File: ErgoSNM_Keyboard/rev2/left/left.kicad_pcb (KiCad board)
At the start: 2 copper layers, 117.5 x 106.7 mm, 113 parts, among them J1 USB_C_Receptacle_USB2.0, J2 Conn_01x10, J3 Conn_01x08, J4 Conn_01x08, Q1 BSS138, SW1 BOOT, SW2 RESET, U1 SRV05-4, U2 RT9013-33GB, U3 RP2040, U4 W25Q128JVS, Y1 12MHz

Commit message: Update rev2
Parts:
- removed the C3 at (66.4, 39.4)
- removed the H4 at (138.4, 88.3)
- removed H7, H9: MountingHole, MountingHole:MountingHole_2.2mm_M2
- removed JP1: SolderJumper_3_Bridged12, Jumper:SolderJumper-3_P1.3mm_Bridged12_Pad1.0x1.5mm_NumberLabels
- removed LD1: SK6812MINI-E, ErgoSNM_Keyboard:SK6812MINI-E
- removed Q1: BSS138, Package_TO_SOT_SMD:SOT-23
- removed the R3 at (83.4, 40.3)
- removed the R4 at (78.1, 40.3)
- added TP4: TestPoint, TestPoint:TestPoint_Pad_D2.5mm, B.Cu at (64.6, 39.1)
- J2: footprint Connector_PinSocket_2.54mm:PinSocket_1x10_P2.54mm_Vertical -> Connector_PinSocket_2.54mm:PinSocket_1x08_P2.54mm_Vertical
- J3: footprint Connector_PinSocket_2.00mm:PinSocket_1x08_P2.00mm_Vertical -> Connector_PinSocket_2.00mm:PinSocket_2x04_P2.00mm_Vertical
- J4: footprint ErgoSNM_Keyboard:FPC_8P_0.5mm -> ErgoSNM_Keyboard:FPC_8P_1.0mm
- TP3: footprint TestPoint:TestPoint_Pad_D2.0mm -> TestPoint:TestPoint_Pad_D2.5mm
- moved R8 114.9 mm to (87.2, 34.2), turned to 0 degrees
- moved C7 113.5 mm to (87.2, 35.2), turned to 180 degrees
- moved C6 112.5 mm to (86.1, 37.2), turned to 0 degrees
- moved C11 112.1 mm to (87.2, 36.2), turned to 180 degrees
- moved C10 111.5 mm to (92.7, 31.0), turned to 180 degrees
- moved R5 109.1 mm to (88.4, 37.2), turned to 0 degrees
- moved Y1 107.8 mm to (87.2, 39.5), turned to 0 degrees
- moved C8 106.4 mm to (97.2, 31.1), turned to 90 degrees
- moved C14 105.0 mm to (98.3, 31.1), turned to 90 degrees
- moved C5 103.1 mm to (88.4, 41.8), turned to 0 degrees
- moved U3 101.3 mm to (94.4, 36.7), turned to 90 degrees
- moved C15 100.5 mm to (100.3, 32.5), turned to 0 degrees
- moved C9 98.8 mm to (100.3, 33.5), turned to 0 degrees
- moved R4 95.9 mm to (101.1, 34.7), turned to 180 degrees
- moved C12 94.9 mm to (93.3, 42.3), turned to -90 degrees
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- renumbered C11 to C10, C12 to C11, C13 to C12, C14 to C13, C15 to C14, C16 to C15, C17 to C16, C4 to C3, C5 to C4, C6 to C5, C7 to C6, C8 to C7, C9 to C8, C10 to C9, H8 to H4, R5 to R3, R6 to R4, R7 to R5, R8 to R6, R9 to R7, R10 to R8
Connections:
- J2 pad 1: GND -> +3V3
- J2 pad 2: CS -> GND
- J2 pad 3: MOSI -> CS
- J2 pad 4: MISO -> MOSI
- J2 pad 5: SCLK -> MISO
- J2 pad 6: Encoder_B -> SCLK
- J2 pad 7: Encoder_A -> Encoder_B
- J2 pad 8: SWCLK -> Encoder_A
- J4 pad 3: ROW_4 -> ROW_0
- J4 pad 4: ROW_3 -> ROW_1
- J4 pad 6: ROW_1 -> ROW_3
- J4 pad 7: ROW_0 -> ROW_4
- KEY29 pad 1: Net-(D29-Pad2) -> COL_5
- KEY29 pad 2: COL_5 -> Net-(D29-Pad2)
- TP3 pad 1: Net-(LD1-Pad2) -> /RP2040/SWCLK
- U3 pad 11: MISO -> unconnected-(U3-Pad11)
- U3 pad 12: CS -> COL_2
- U3 pad 13: SCLK -> COL_1
- U3 pad 14: MOSI -> COL_0
- U3 pad 15: SERIAL -> unconnected-(U3-Pad15)
- U3 pad 18: unconnected-(U3-Pad18) -> +3V3
- U3 pad 24: SWCLK -> /RP2040/SWCLK
- U3 pad 25: SWDIO -> /RP2040/SWDIO
- U3 pad 28: Encoder_B -> COL_6
- U3 pad 29: Encoder_A -> Encoder_B
- U3 pad 3: COL_4 -> unconnected-(U3-Pad3)
- U3 pad 30: RGB_LED_DATA_3V3 -> Encoder_A
- U3 pad 31: Handedness -> MISO
- U3 pad 32: unconnected-(U3-Pad32) -> CS
- U3 pad 34: unconnected-(U3-Pad34) -> SCLK
- U3 pad 35: COL_6 -> MOSI
- U3 pad 36: ROW_0 -> ROW_4
- U3 pad 37: ROW_1 -> ROW_3
- U3 pad 39: ROW_3 -> ROW_1
- U3 pad 4: COL_0 -> unconnected-(U3-Pad4)
- U3 pad 40: ROW_4 -> ROW_0
- U3 pad 5: COL_1 -> SERIAL
- U3 pad 6: COL_2 -> COL_5
- U3 pad 7: COL_3 -> COL_4
- U3 pad 8: COL_5 -> COL_3
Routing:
- net RGB_LED_DATA_3V3: track 222.6 -> 0.00 mm, vias 2 -> 0
- net CS: track 18.8 -> 186.1 mm
- net SCLK: track 14.1 -> 179.1 mm, vias 0 -> 1
- net MOSI: track 21.4 -> 186.3 mm, vias 0 -> 1
- net MISO: track 16.9 -> 171.8 mm, vias 0 -> 1
- net COL_6: track 20.6 -> 171.1 mm, vias 1 -> 2
- net Encoder_A: track 17.7 -> 162.6 mm, vias 0 -> 2
- net Encoder_B: track 19.1 -> 163.8 mm, vias 0 -> 2
- net +5V: track 235.4 -> 114.6 mm, vias 3 -> 0
- net COL_0: track 218.9 -> 109.0 mm, vias 1 -> 3
- net COL_1: track 197.9 -> 89.6 mm
- net ROW_4: track 133.2 -> 221.0 mm, vias 5 -> 2
- net COL_2: track 174.5 -> 97.5 mm
- net /USB_D-: track 102.8 -> 47.0 mm
- net /USB_D+: track 102.2 -> 47.6 mm
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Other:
- board size 117.5 x 106.7 mm -> 115.6 x 106.7 mm

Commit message: Add logo
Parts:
- added G***: LOGO, LOGO, F.Cu at (88.6, 33.3)
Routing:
- net +3V3: track 252.2 -> 251.6 mm

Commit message: Update BOM, net, placement, etc.
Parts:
- removed the J3 at (160.0, 109.7)
- added LD1: Red, LED_SMD:LED_0603_1608Metric, B.Cu at (62.4, 38.9)
- added R3: 1k, Resistor_SMD:R_0402_1005Metric, B.Cu at (62.4, 41.4)
- added R4: 5.1k, Resistor_SMD:R_0402_1005Metric, B.Cu at (96.3, 42.1)
- added TP1: TestPoint, TestPoint:TestPoint_Pad_D2.5mm, B.Cu at (150.5, 32.7)
- added TP4: TestPoint, TestPoint:TestPoint_Pad_D2.5mm, B.Cu at (154.2, 32.7)
- G***: moved to B.Cu
- J2: value Conn_01x10 -> USB_C_Receptacle_USB2.0; footprint Connector_PinSocket_2.54mm:PinSocket_1x08_P2.54mm_Vertical -> Connector_USB:USB_C_Receptacle_HRO_TYPE-C-31-M-12
- J3: renamed from TRRS1; footprint ErgoSNM_Keyboard:PJ-393 -> ErgoSNM_Keyboard:PJ-393 8P TRRS
- J4: footprint ErgoSNM_Keyboard:FPC_8P_1.0mm -> Connector_JST:JST_GH_SM08B-GHS-TB_1x08-1MP_P1.25mm_Horizontal
- moved G*** 102.2 mm to (171.1, 93.7), turned to 180 degrees
- moved J2 73.4 mm to (174.2, 55.8), turned to -90 degrees
- moved J3 16.3 mm to (171.6, 74.2), turned to 0 degrees
- moved J4 0.88 mm to (163.5, 116.2)
- moved TP6 0.76 mm to (65.4, 39.1)
- moved TP5 0.53 mm to (69.0, 39.1)
- moved C14 0.38 mm to (97.4, 42.1)
- renumbered C8 to C10, C10 to C11, C11 to C12, C12 to C13, C13 to C14, C14 to C15, C15 to C16, C16 to C3, C5 to C4, C6 to C5, C3 to C6, C9 to C8, C4 to C9, D17 to D10, D22 to D11, D27 to D12, D3 to D13, D8 to D14, D13 to D15, D18 to D16, D23 to D17, D28 to D18, D4 to D19, D6 to D2, D9 to D20, D14 to D21, D19 to D22, D24 to D23, D29 to D24, D5 to D25, D10 to D26, D15 to D27, D20 to D28, D25 to D29, D11 to D3, D16 to D4, D21 to D5, D26 to D6, D2 to D7, D7 to D8, D12 to D9, KEY17 to KEY10, KEY22 to KEY11, KEY27 to KEY12, KEY3 to KEY13, KEY8 to KEY14, KEY13 to KEY15, KEY18 to KEY16, KEY23 to KEY17, KEY28 to KEY18, KEY4 to KEY19, KEY6 to KEY2, KEY9 to KEY20, KEY14 to KEY21, KEY19 to KEY22, KEY24 to KEY23, KEY29 to KEY24, KEY5 to KEY25, KEY10 to KEY26, KEY15 to KEY27, KEY20 to KEY28, KEY25 to KEY29, KEY11 to KEY3, KEY16 to KEY4, KEY21 to KEY5, KEY26 to KEY6, KEY2 to KEY7, KEY7 to KEY8, KEY12 to KEY9, R8 to R10, R3 to R5, R4 to R6, R6 to R7, R7 to R8, R5 to R9, TP1 to TP2, TP2 to TP3, TP3 to TP5, TP4 to TP6, U2 to U1, U1 to U2, U4 to U3, U3 to U4
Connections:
- J4 pad 1: COL_6 -> COL_5
- J4 pad 2: COL_5 -> ROW_4
- J4 pad 3: ROW_0 -> ROW_5
- J4 pad 4: ROW_1 -> COL_7
- J4 pad 5: ROW_2 -> COL_6
- J4 pad 6: ROW_3 -> Encoder_A
- J4 pad 7: ROW_4 -> Encoder_B
- U4 pad 2: unconnected-(U3-Pad2) -> SERIAL
- U4 pad 28: COL_6 -> STATE_LED
- U4 pad 30: Encoder_A -> unconnected-(U4-Pad30)
- U4 pad 31: MISO -> ROW_5
- U4 pad 32: CS -> COL_7
- U4 pad 34: SCLK -> COL_6
- U4 pad 35: MOSI -> Encoder_A
- U4 pad 5: SERIAL -> unconnected-(U4-Pad5)
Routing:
- net COL_7: track 0.00 -> 205.0 mm, vias 0 -> 2
- net ROW_5: track 0.00 -> 199.4 mm, vias 0 -> 2
- net MOSI: track 186.3 -> 0.00 mm, vias 1 -> 0
- net CS: track 186.1 -> 0.00 mm, vias 1 -> 0
- net SCLK: track 179.1 -> 0.00 mm, vias 1 -> 0
- net MISO: track 171.8 -> 0.00 mm, vias 1 -> 0
- net ROW_0: track 225.5 -> 146.9 mm, vias 7 -> 6
- net ROW_1: track 221.2 -> 160.9 mm, vias 3 -> 2
- net SERIAL: track 86.1 -> 136.3 mm
- net +5V: track 114.6 -> 65.2 mm
- net +3V3: track 251.6 -> 204.2 mm, vias 5 -> 8
- net Encoder_A: track 162.6 -> 208.6 mm
- net ROW_2: track 227.6 -> 182.3 mm, vias 3 -> 2
- net STATE_LED: track 0.00 -> 38.1 mm
- net COL_6: track 171.1 -> 208.1 mm
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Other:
- outline, holes or cut-outs redrawn
- board text added: "ErgoSNM"
- board text added: "LEFT"

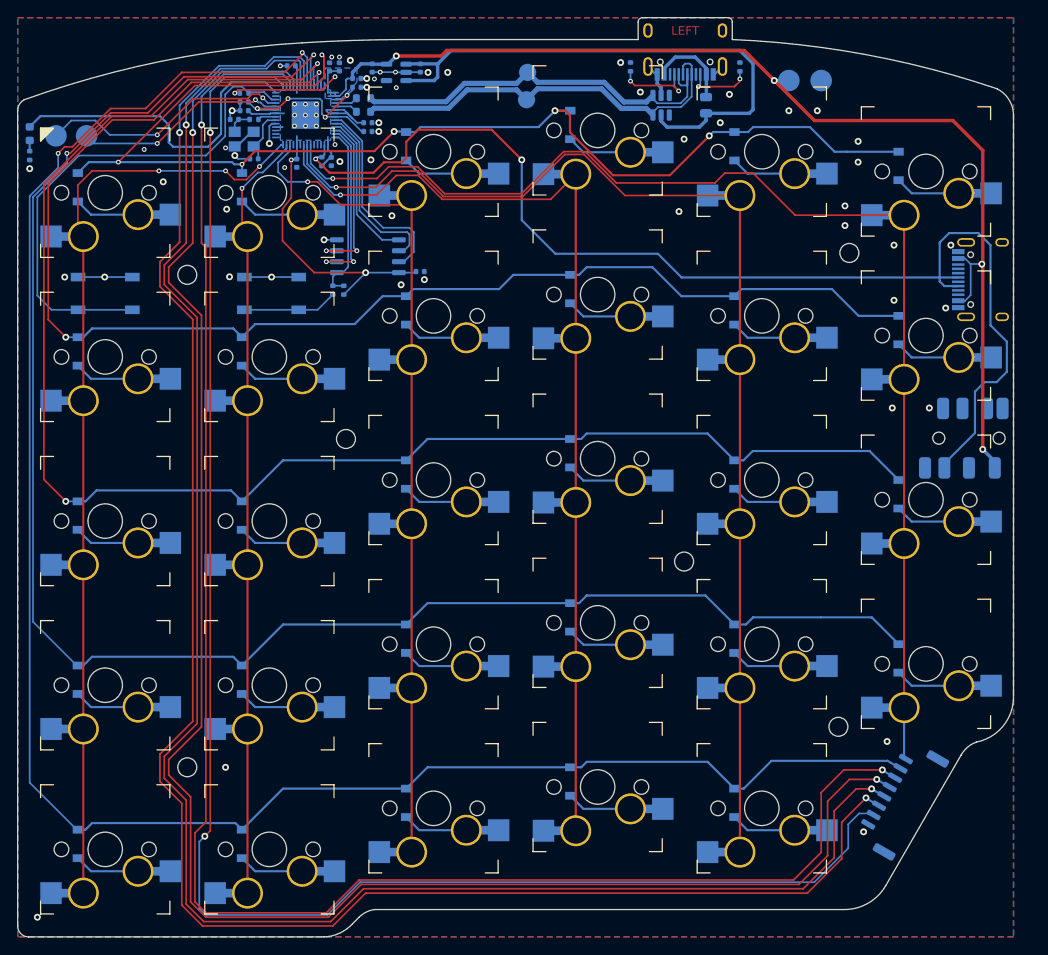
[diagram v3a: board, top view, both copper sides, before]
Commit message: Update RT9013 LDO placement and add logo
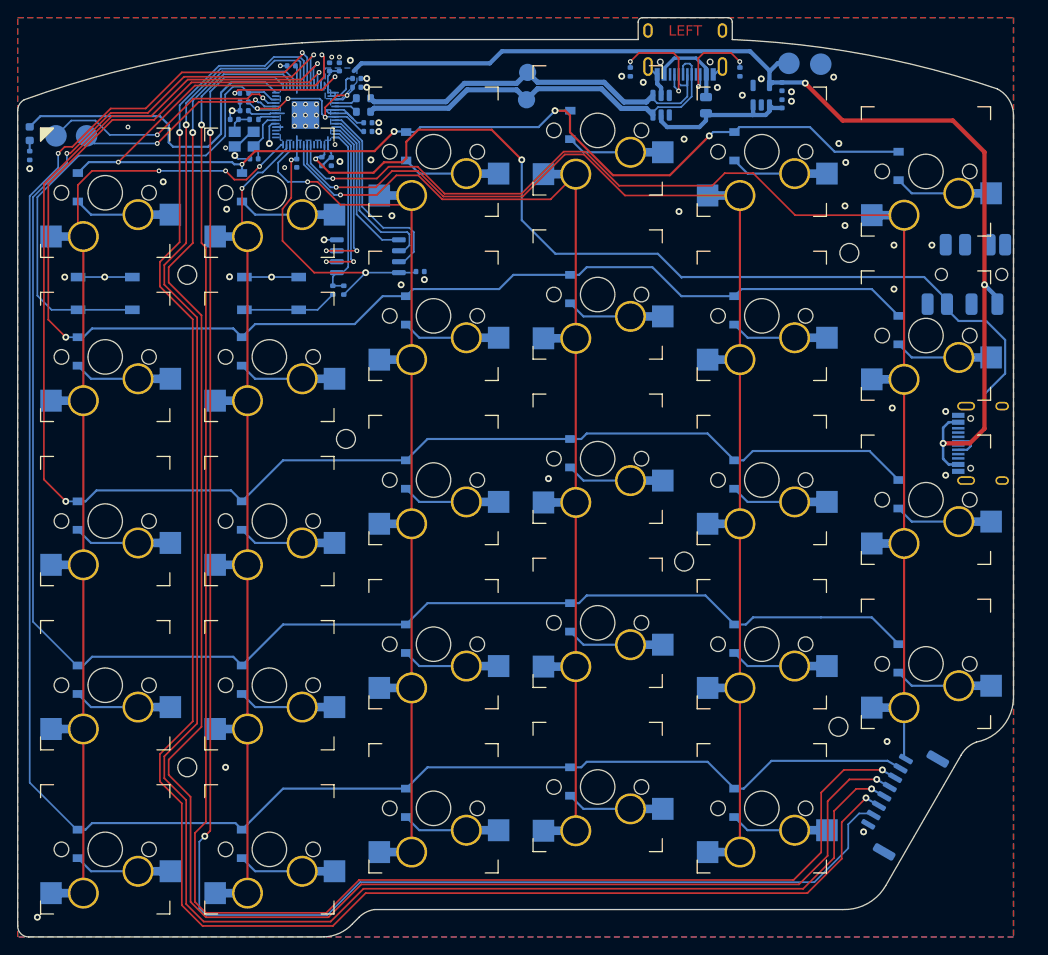
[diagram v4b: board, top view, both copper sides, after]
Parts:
- added kibuzzard-63A148C1: G***, kibuzzard-63A148C1, B.Cu at (164.0, 38.7)
- moved G*** 56.8 mm to (171.6, 36.9)
- moved C2 47.6 mm to (149.7, 33.4)
- moved U1 42.4 mm to (147.3, 34.4), turned to 90 degrees
- moved C1 42.2 mm to (149.7, 35.4), turned to 90 degrees
- moved J3 19.0 mm to (171.9, 55.2)
- moved J2 19.0 mm to (174.2, 74.8)
- moved TP1 2.00 mm to (150.5, 30.7)
- moved TP4 1.90 mm to (154.2, 30.8)
- moved R1 0.59 mm to (132.1, 31.7), turned to -90 degrees
- moved R2 0.59 mm to (144.8, 31.7), turned to -90 degrees
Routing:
- net +5V: track 65.2 -> 18.5 mm
- net SERIAL: track 136.3 -> 118.2 mm
- net GND: track 36.5 -> 30.9 mm, vias 65 -> 62
- net +3V3: track 204.2 -> 207.8 mm, vias 8 -> 7
- net Net-(J1-PadA5): track 9.33 -> 12.9 mm
- net Net-(J1-PadB5): track 7.74 -> 11.0 mm
- net +1V1: track 25.3 -> 26.0 mm
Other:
- board text removed: "ErgoSNM"

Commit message: Update left
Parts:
- moved H5 1.26 mm to (156.8, 51.6)
- moved H6 1.24 mm to (156.8, 108.8)
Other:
- outline, holes or cut-outs redrawn
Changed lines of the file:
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@@
     (grid_origin 60.96 25.4)
     (pcbplotparams
-      (layerselection 0x00010fc_ffffffff)
+      (layerselection 0x0000100_7ffffffe)
       (disableapertmacros false)
       (usegerberextensions true)
@@
       (svguseinch false)
       (svgprecision 6)
-      (excludeedgelayer true)
+      (excludeedgelayer false)
       (plotframeref false)
       (viasonmask false)
       (mode 1)
-      (useauxorigin false)
+      (useauxorigin true)
       (hpglpennumber 1)
       (hpglpenspeed 20)
       (hpglpendiameter 15.000000)
-      (dxfpolygonmode true)
-      (dxfimperialunits true)
+      (dxfpolygonmode false)
+      (dxfimperialunits false)
       (dxfusepcbnewfont true)
       (psnegative false)
       (psa4output false)
-      (plotreference true)
+      (plotreference false)
       (plotvalue false)
       (plotinvisibletext false)
       (sketchpadsonfab false)
       (subtractmaskfromsilk true)
-      (outputformat 1)
+      (outputformat 3)
       (mirror false)
       (drillshape 0)
@@
   )
   (footprint "MountingHole:MountingHole_2.2mm_M2" (layer "B.Cu")
-    (at 156.21 107.696 180)
+    (at 156.845 108.7628 180)
     (descr "Mounting Hole 2.2mm, no annular, M2")
     (tags "mounting hole 2.2mm no annular m2")
@@
     (attr board_only exclude_from_pos_files exclude_from_bom)
     (fp_text reference "kibuzzard-63A148C1" (at 0 3.821906) (layer "B.SilkS") hide
-      (effects (font (size 0 0)) (justify mirror))
+      (effects (font (size 0 0) (thickness 0.15)) (justify mirror))
     )
     (fp_text value "G***" (at 0 -3.821906) (layer "B.SilkS") hide
-      (effects (font (size 0 0)) (justify mirror))
+      (effects (font (size 0 0) (thickness 0.15)) (justify mirror))
     )
     (fp_poly (pts
@@
   )
   (footprint "MountingHole:MountingHole_2.2mm_M2" (layer "B.Cu")
-    (at 157.48 52.705 180)
+    (at 156.845 51.6128 180)
     (descr "Mounting Hole 2.2mm, no annular, M2")
     (tags "mounting hole 2.2mm no annular m2")
@@
   (gr_arc (start 62.23 132.08) (mid 61.331974 131.708026) (end 60.96 130.81) (layer "Edge.Cuts") (width 0.1))
   (gr_arc (start 99.822 130.556) (mid 98.323259 131.647895) (end 96.52 132.08) (layer "Edge.Cuts") (width 0.1))
+  (gr_arc (start 176.53 104.394) (mid 176.418408 104.663408) (end 176.149 104.775) (layer "Edge.Cuts") (width 0.1))
   (gr_line (start 102.362 128.905) (end 156.718 128.905) (layer "Edge.Cuts") (width 0.1))
   (gr_line (start 132.969 27.94) (end 105.41 27.94) (layer "Edge.Cuts") (width 0.1))
   (gr_arc (start 161.70275 126.125855) (mid 159.596418 128.207848) (end 156.718 128.905) (layer "Edge.Cuts") (width 0.1))
   (gr_line (start 99.822 130.556) (end 100.584 129.794) (layer "Edge.Cuts") (width 0.1))
-  (gr_arc (start 176.53 104.394) (mid 175.260735 107.690274) (end 172.212 109.474) (layer "Edge.Cuts") (width 0.1))
+  (gr_line (start 176.149 104.775) (end 173.99 104.775) (layer "Edge.Cuts") (width 0.1))
   (gr_line (start 132.969 25.908) (end 132.969 27.94) (layer "Edge.Cuts") (width 0.1))
   (gr_line (start 60.96 36.195) (end 60.96 130.81) (layer "Edge.Cuts") (width 0.1))
-  (gr_arc (start 170.434 110.998) (mid 171.187248 110.077614) (end 172.212 109.474) (layer "Edge.Cuts") (width 0.1))
   (gr_arc (start 132.969 25.908) (mid 133.11779 25.54879) (end 133.477 25.4) (layer "Edge.Cuts") (width 0.1))
   (gr_line (start 62.23 132.08) (end 96.52 132.08) (layer "Edge.Cuts") (width 0.1))
@@
   (gr_arc (start 60.96 36.195) (mid 61.165114 35.454469) (end 61.722 34.925) (layer "Edge.Cuts") (width 0.1))
   (gr_arc (start 143.383 25.4) (mid 143.74221 25.54879) (end 143.891 25.908) (layer "Edge.Cuts") (width 0.1))
-  (gr_line (start 170.434 110.998) (end 161.70275 126.125855) (layer "Edge.Cuts") (width 0.1))
+  (gr_line (start 173.99 104.775) (end 161.70275 126.125855) (layer "Edge.Cuts") (width 0.1))
   (gr_arc (start 93.98 28.321) (mid 99.692247 28.047912) (end 105.41 27.94) (layer "Edge.Cuts") (width 0.1))
   (gr_arc locked (start 185.006816 145.274159) (mid 184.773815 144.970551) (end 184.823803 144.591146) (layer "User.9") (width 0.15))
@@
   (via (at 98.36 42.1) (size 0.8) (drill 0.4) (layers "F.Cu" "B.Cu") (net 2))
   (via (at 101.473 32.4612) (size 0.8) (drill 0.4) (layers "F.Cu" "B.Cu") (net 2))
-  (via (at 156.972 47.244) (size 0.8) (drill 0.4) (layers "F.Cu" "B.Cu") (free) (net 2))
+  (via (at 156.8704 47.2948) (size 0.8) (drill 0.4) (layers "F.Cu" "B.Cu") (free) (net 2))
   (via (at 108.16 55.8) (size 0.8) (drill 0.4) (layers "F.Cu" "B.Cu") (net 2))
   (via (at 94.361 37.973) (size 0.56) (drill 0.3) (layers "F.Cu" "B.Cu") (net 2))
@@
   (via (at 98.298 29.972) (size 0.56) (drill 0.3) (layers "F.Cu" "B.Cu") (net 2))
   (via (at 94.361 35.433) (size 0.56) (drill 0.3) (layers "F.Cu" "B.Cu") (net 2))
-  (via (at 156.972 49.53) (size 0.8) (drill 0.4) (layers "F.Cu" "B.Cu") (free) (net 2))
+  (via (at 156.8704 49.3268) (size 0.8) (drill 0.4) (layers "F.Cu" "B.Cu") (free) (net 2))
   (via (at 122.56 78.9) (size 0.8) (drill 0.4) (layers "F.Cu" "B.Cu") (free) (net 2))
   (via (at 96.52 51.181) (size 0.8) (drill 0.4) (layers "F.Cu" "B.Cu") (net 2))
